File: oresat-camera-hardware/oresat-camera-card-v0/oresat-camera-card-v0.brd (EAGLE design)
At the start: 99.8 x 94.7 mm, 318 parts, among them J1 J-SAMTEC-TFM-120-X1-XXX-D-RA, J2 DM3BT-DSF-PEJS, J4 3-1734592-64-1734592-0, J8 2-1734592-0, Q1 DMP2240UDM, Q3 MIC842, Q4 MIC842, Q5 PMV45EN, Q6 MOSFET-PCH-SOT23-6, Q7 MOSFET-PCH-SOT23-6, Q8 PMV45EN, Q9 MMBT2907, U1 MAX7310ATE, U10 SN74LVC8T245MPWREPPW24-M, U11 RCLAMP0504FB, U12 RCLAMP0504FB, U13 TPS2051CDBVR, U14 TLVH431, U15 SN74LVC1G07DCK, U2 TPS62112, U3 MAX4211CETE, U4 TCAN330, U5 CLVCH16T245MDGGREP, U6 OSD3358-512M-BSM, U7 TCA9509DGKRDGK8-M, U9 TLV70028QDDCRQ1, Y1 24MHz

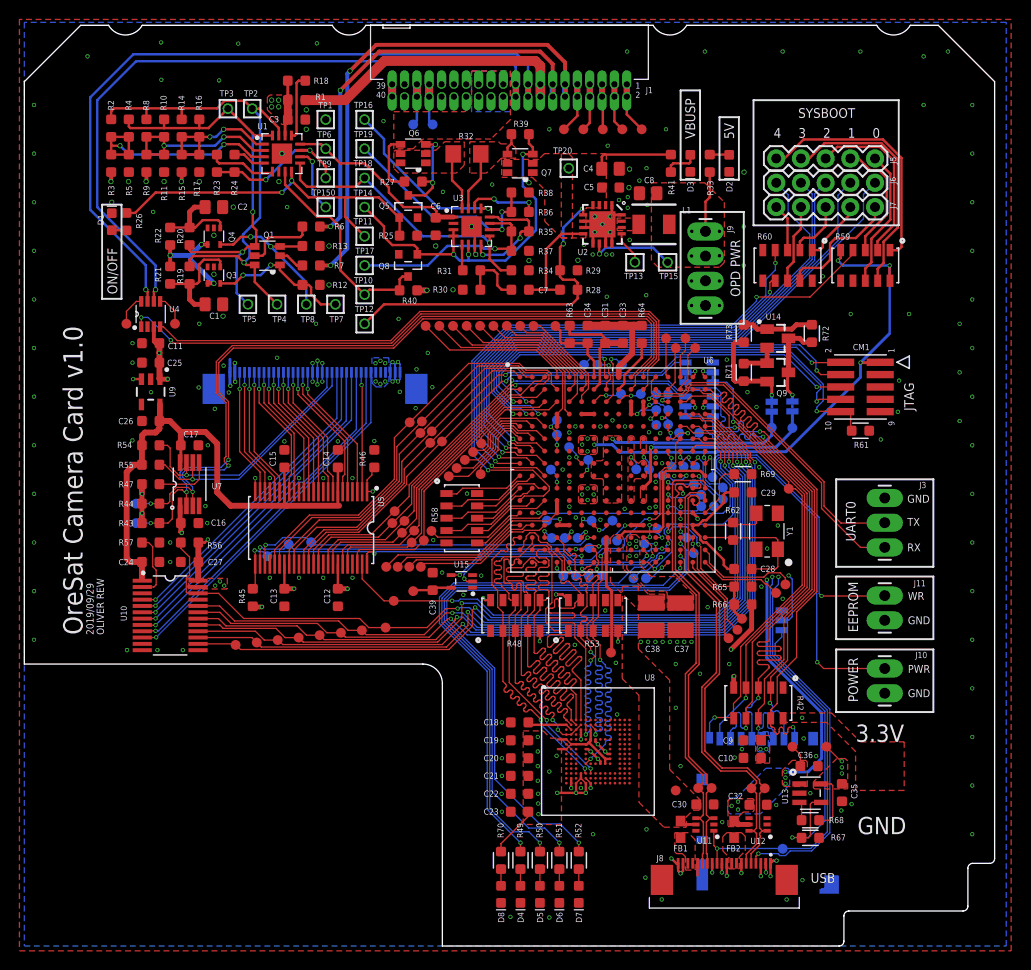
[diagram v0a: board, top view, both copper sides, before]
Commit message: moar VIAS
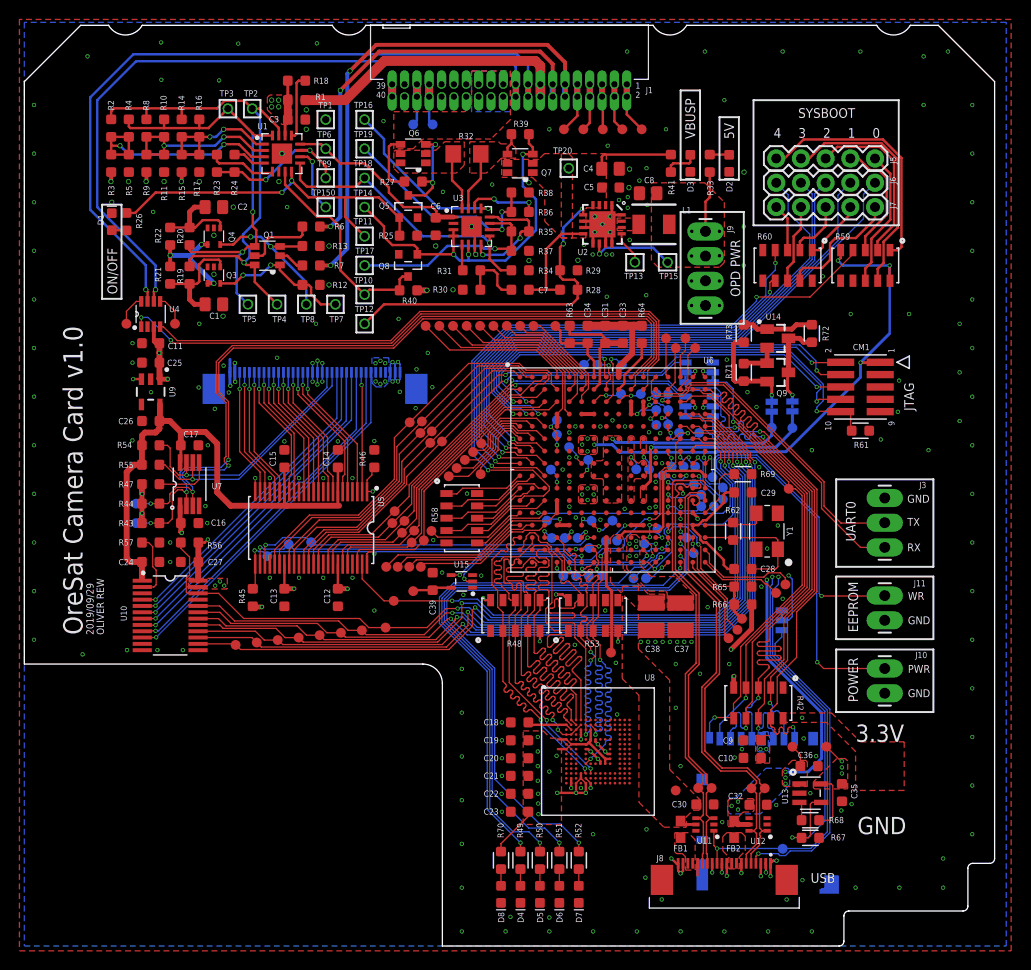
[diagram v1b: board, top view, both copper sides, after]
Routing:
- net GND: vias 244 -> 268
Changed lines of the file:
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@@
 <setting verticaltext="up"/>
 </settings>
-<grid distance="0.5" unitdist="mm" unit="mm" style="lines" multiple="1" display="yes" altdistance="0.0625" altunitdist="mm" altunit="mm"/>
+<grid distance="1.5" unitdist="mm" unit="mm" style="lines" multiple="1" display="yes" altdistance="0.0625" altunitdist="mm" altunit="mm"/>
 <layers>
 <layer number="1" name="Top" color="4" fill="1" visible="yes" active="yes"/>
@@
 <via x="36.9375" y="84.84375" extent="1-16" drill="0.254"/>
 <via x="26.1875" y="78.625" extent="1-16" drill="0.35"/>
+<via x="45" y="1.5" extent="1-16" drill="0.254"/>
+<via x="49.5" y="1.5" extent="1-16" drill="0.254"/>
+<via x="54" y="1.5" extent="1-16" drill="0.254"/>
+<via x="58.5" y="1.5" extent="1-16" drill="0.254"/>
+<via x="63" y="1.5" extent="1-16" drill="0.254"/>
+<via x="67.5" y="1.5" extent="1-16" drill="0.254"/>
+<via x="72" y="1.5" extent="1-16" drill="0.254"/>
+<via x="76.5" y="1.5" extent="1-16" drill="0.254"/>
+<via x="81" y="1.5" extent="1-16" drill="0.254"/>
+<via x="85.5" y="6" extent="1-16" drill="0.254"/>
+<via x="90" y="6" extent="1-16" drill="0.254"/>
+<via x="94.5" y="6" extent="1-16" drill="0.254"/>
+<via x="94.5" y="9" extent="1-16" drill="0.254"/>
+<via x="45" y="6" extent="1-16" drill="0.254"/>
+<via x="45" y="10.5" extent="1-16" drill="0.254"/>
+<via x="45" y="15" extent="1-16" drill="0.254"/>
+<via x="45" y="19.5" extent="1-16" drill="0.254"/>
+<via x="45" y="24" extent="1-16" drill="0.254"/>
+<via x="45" y="28.5" extent="1-16" drill="0.254"/>
+<via x="6" y="30" extent="1-16" drill="0.254"/>
+<via x="36" y="34.5" extent="1-16" drill="0.254"/>
+<via x="81" y="51" extent="1-16" drill="0.254"/>
+<via x="93" y="51" extent="1-16" drill="0.254"/>
+<via x="72" y="87" extent="1-16" drill="0.254"/>
 </signal>
 <signal name="N$262">

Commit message: small improvements
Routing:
- net N$585: track 48.5 -> 51.2 mm
- net CAN2_L: track 72.5 -> 71.7 mm
- net CAN2_H: track 75.3 -> 74.4 mm
- net VPD: track 51.4 -> 50.9 mm
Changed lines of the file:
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@@
 </element>
 <element name="D1" library="SparkFun-LED" library_urn="urn:adsk.eagle:library:529" package="LED-0603" package3d_urn="urn:adsk.eagle:package:39354/1" value="AMBER" x="9" y="74.5" smashed="yes" rot="R90">
-<attribute name="NAME" x="8.1775" y="74.6875" size="0.635" layer="25" font="vector" ratio="20" rot="R90" align="bottom-center"/>
+<attribute name="NAME" x="7.6775" y="74.5" size="0.635" layer="25" font="vector" ratio="20" rot="R90" align="bottom-center"/>
 <attribute name="PROD_ID" value="" x="146.5" y="49.5" size="1.778" layer="27" rot="R90" display="off"/>
 <attribute name="VALUE" x="9.635" y="74.5" size="0.6096" layer="27" font="vector" ratio="20" rot="R90" align="top-center"/>
@@
 <wire x1="13.5" y1="67.5" x2="13.5" y2="70" width="0.254" layer="16"/>
 <wire x1="13.5" y1="70" x2="7.5" y2="76" width="0.254" layer="16"/>
-<wire x1="7.5" y1="76" x2="7.5" y2="87" width="0.254" layer="16"/>
-<wire x1="11.5" y1="91" x2="7.5" y2="87" width="0.254" layer="16"/>
+<wire x1="7.5" y1="76" x2="7.5" y2="85.5" width="0.254" layer="16"/>
+<wire x1="13" y1="91" x2="7.5" y2="85.5" width="0.254" layer="16"/>
 <wire x1="50.535" y1="88.629" x2="50.535" y2="90.465" width="0.254" layer="16"/>
 <wire x1="50.535" y1="90.465" x2="50" y2="91" width="0.254" layer="16"/>
-<wire x1="50" y1="91" x2="11.5" y2="91" width="0.254" layer="16"/>
+<wire x1="50" y1="91" x2="13" y2="91" width="0.254" layer="16"/>
 <wire x1="50.535" y1="87.359" x2="50.535" y2="88.629" width="0.6096" layer="1"/>
 <wire x1="50.535" y1="87.359" x2="50.535" y2="88.629" width="0.6096" layer="16"/>
@@
 <wire x1="51.805" y1="90.60125" x2="51.805" y2="88.629" width="0.254" layer="16"/>
 <wire x1="12.5" y1="70" x2="6.78125" y2="75.71875" width="0.254" layer="16"/>
-<wire x1="6.78125" y1="75.71875" x2="6.78125" y2="87.28125" width="0.254" layer="16"/>
-<wire x1="6.78125" y1="87.28125" x2="11.21875" y2="91.71875" width="0.254" layer="16"/>
-<wire x1="11.21875" y1="91.71875" x2="50.6875" y2="91.71875" width="0.254" layer="16"/>
+<wire x1="6.78125" y1="75.71875" x2="6.78125" y2="85.78125" width="0.254" layer="16"/>
+<wire x1="6.78125" y1="85.78125" x2="12.71875" y2="91.71875" width="0.254" layer="16"/>
+<wire x1="12.71875" y1="91.71875" x2="50.6875" y2="91.71875" width="0.254" layer="16"/>
 <wire x1="50.6875" y1="91.71875" x2="51.805" y2="90.60125" width="0.254" layer="16"/>
 <wire x1="51.805" y1="87.359" x2="51.805" y2="88.629" width="0.6096" layer="1"/>
@@
 <wire x1="49.94" y1="63.3565" x2="73.0604375" y2="63.3565" width="0.127" layer="16"/>
 <contactref element="R60" pad="7"/>
-<wire x1="76.6875" y1="67.25" x2="76.6875" y2="66.9835625" width="0.127" layer="16"/>
-<wire x1="76.6875" y1="66.9835625" x2="73.0604375" y2="63.3565" width="0.127" layer="16"/>
-<via x="76.6875" y="67.25" extent="1-16" drill="0.254"/>
-<wire x1="76.6875" y1="67.25" x2="76.6875" y2="68.2577" width="0.127" layer="1"/>
-<wire x1="76.855" y1="68.4252" x2="76.6875" y2="68.2577" width="0.127" layer="1"/>
-<wire x1="76.855" y1="68.4252" x2="77.23" y2="68.4252" width="0.127" layer="1"/>
+<wire x1="77.875" y1="69.5" x2="77.875" y2="68.1710625" width="0.127" layer="16"/>
+<wire x1="77.875" y1="68.1710625" x2="73.0604375" y2="63.3565" width="0.127" layer="16"/>
+<via x="77.875" y="69.5" extent="1-16" drill="0.254"/>
+<wire x1="77.875" y1="69.5" x2="77.4375" y2="69.5" width="0.127" layer="1"/>
+<wire x1="77.23" y1="69.2925" x2="77.23" y2="68.4252" width="0.127" layer="1"/>
+<wire x1="77.4375" y1="69.5" x2="77.23" y2="69.2925" width="0.127" layer="1"/>
 </signal>
 <signal name="N$586">
@@
 <contactref element="R60" pad="4"/>
 <via x="77.25" y="70.25" extent="1-16" drill="0.254"/>
-<wire x1="76.2684" y1="68.5486" x2="77.25" y2="69.5302" width="0.127" layer="16"/>
-<wire x1="76.2684" y1="66.923675" x2="76.2684" y2="68.5486" width="0.127" layer="16"/>
-<wire x1="72.955225" y1="63.6105" x2="76.2684" y2="66.923675" width="0.127" layer="16"/>
-<wire x1="77.25" y1="69.5302" x2="77.25" y2="70.25" width="0.127" layer="16"/>
+<wire x1="77.25" y1="67.905275" x2="77.25" y2="70.25" width="0.127" layer="16"/>
+<wire x1="72.955225" y1="63.6105" x2="77.25" y2="67.905275" width="0.127" layer="16"/>
 <wire x1="77.25" y1="70.25" x2="77.23" y2="70.27" width="0.127" layer="1"/>
 <wire x1="77.23" y1="70.27" x2="77.23" y2="71.5748" width="0.127" layer="1"/>
@@
 <wire x1="49.729575" y1="63.8645" x2="72.8500125" y2="63.8645" width="0.127" layer="16"/>
 <contactref element="R59" pad="4"/>
-<wire x1="75.3125125" y1="66.327" x2="75.3125" y2="66.75" width="0.127" layer="16"/>
-<via x="75.3125" y="66.75" extent="1-16" drill="0.254"/>
-<wire x1="72.8500125" y1="63.8645" x2="75.3125125" y2="66.327" width="0.127" layer="16"/>
-<wire x1="75.3125" y1="66.75" x2="80.8125" y2="66.75" width="0.127" layer="1"/>
+<wire x1="75.8125125" y1="66.827" x2="75.8125" y2="67.25" width="0.127" layer="16"/>
+<via x="75.8125" y="67.25" extent="1-16" drill="0.254"/>
+<wire x1="72.8500125" y1="63.8645" x2="75.8125125" y2="66.827" width="0.127" layer="16"/>
+<wire x1="75.8125" y1="67.25" x2="81.3125" y2="67.25" width="0.127" layer="1"/>
 <wire x1="85.23" y1="71.1675" x2="85.23" y2="71.5748" width="0.127" layer="1"/>
-<wire x1="80.8125" y1="66.75" x2="85.23" y2="71.1675" width="0.127" layer="1"/>
+<wire x1="81.3125" y1="67.25" x2="85.23" y2="71.1675" width="0.127" layer="1"/>
 </signal>
 <signal name="N$602">
@@
 <wire x1="82.875" y1="72.25" x2="82.875" y2="70.5625" width="0.254" layer="1"/>
 <wire x1="82.875" y1="70.5625" x2="82.0625" y2="69.75" width="0.254" layer="1"/>
-<wire x1="79.77" y1="69.395" x2="79.77" y2="68.4252" width="0.254" layer="1"/>
+<wire x1="79.77" y1="69.2075" x2="79.77" y2="68.4252" width="0.254" layer="1"/>
 <wire x1="87.5" y1="74.78881875" x2="85.52368125" y2="72.8125" width="0.254" layer="1"/>
 <wire x1="85.52368125" y1="72.8125" x2="83.4375" y2="72.8125" width="0.254" layer="1"/>
 <wire x1="83.4375" y1="72.8125" x2="82.875" y2="72.25" width="0.254" layer="1"/>
-<wire x1="82.0625" y1="69.75" x2="80.125" y2="69.75" width="0.254" layer="1"/>
-<wire x1="80.125" y1="69.75" x2="79.77" y2="69.395" width="0.254" layer="1"/>
+<wire x1="82.0625" y1="69.75" x2="80.3125" y2="69.75" width="0.254" layer="1"/>
+<wire x1="80.3125" y1="69.75" x2="79.77" y2="69.2075" width="0.254" layer="1"/>
 </signal>
 <signal name="N$631">
@@
 <wire x1="25.96875" y1="85" x2="25.4375" y2="85.53125" width="1.016" layer="15"/>
 <wire x1="31" y1="85" x2="32.5" y2="83.5" width="0.6096" layer="15"/>
-<wire x1="36.28125" y1="83.5" x2="40.0625" y2="79.71875" width="0.6096" layer="15"/>
-<wire x1="40.0625" y1="79.71875" x2="40.0625" y2="68.78125" width="0.6096" layer="15"/>
+<wire x1="35.40625" y1="83.5" x2="40.0625" y2="78.84375" width="0.6096" layer="15"/>
+<wire x1="40.0625" y1="78.84375" x2="40.0625" y2="68.78125" width="0.6096" layer="15"/>
 <wire x1="40.0625" y1="68.78125" x2="41.40625" y2="67.4375" width="0.6096" layer="15"/>
 <via x="41.40625" y="67.4375" extent="1-16" drill="0.35"/>
-<wire x1="32.5" y1="83.5" x2="36.28125" y2="83.5" width="0.6096" layer="15"/>
+<wire x1="32.5" y1="83.5" x2="35.40625" y2="83.5" width="0.6096" layer="15"/>
 <wire x1="40.4" y1="67.4375" x2="41.40625" y2="67.4375" width="0.6096" layer="1"/>
 <wire x1="8.9375" y1="79.6" x2="8.9375" y2="78.65625" width="0.4064" layer="1"/>
@@
 <wire x1="16.1875" y1="79.6" x2="16.1875" y2="78.65625" width="0.4064" layer="1"/>
 <wire x1="16.1875" y1="78.65625" x2="16.15625" y2="78.625" width="0.4064" layer="1"/>
+<wire x1="26.15625" y1="86.3125" x2="26.15625" y2="87" width="0" layer="19" extent="1-1"/>
+<wire x1="25.4375" y1="87" x2="26.15625" y2="87" width="0" layer="19" extent="1-1"/>
+<wire x1="25.4375" y1="86.3125" x2="25.4375" y2="87" width="0" layer="19" extent="1-1"/>
+<wire x1="27.1" y1="87" x2="26.15625" y2="87" width="0" layer="19" extent="1-1"/>
+<wire x1="16.1875" y1="79.6" x2="26.825" y2="83.3596" width="0" layer="19" extent="1-1"/>
+<wire x1="12.5625" y1="79.6" x2="16.1875" y2="79.6" width="0" layer="19" extent="1-1"/>
+<wire x1="8.9375" y1="79.6" x2="12.5625" y2="79.6" width="0" layer="19" extent="1-1"/>
+<wire x1="15" y1="72.1" x2="16.15625" y2="78.625" width="0" layer="19" extent="1-1"/>
 </signal>
 <signal name="PB6/SCL">

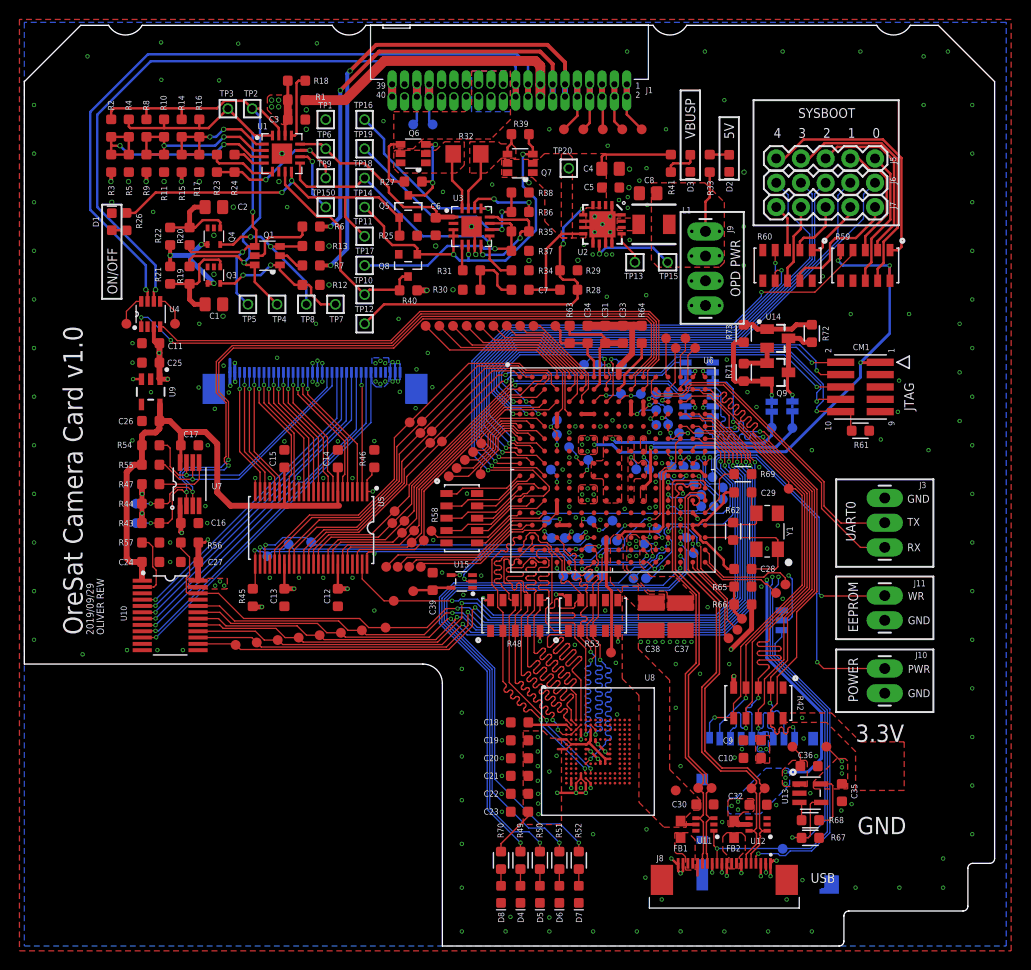
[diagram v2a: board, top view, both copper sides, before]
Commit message: added silk on resistors
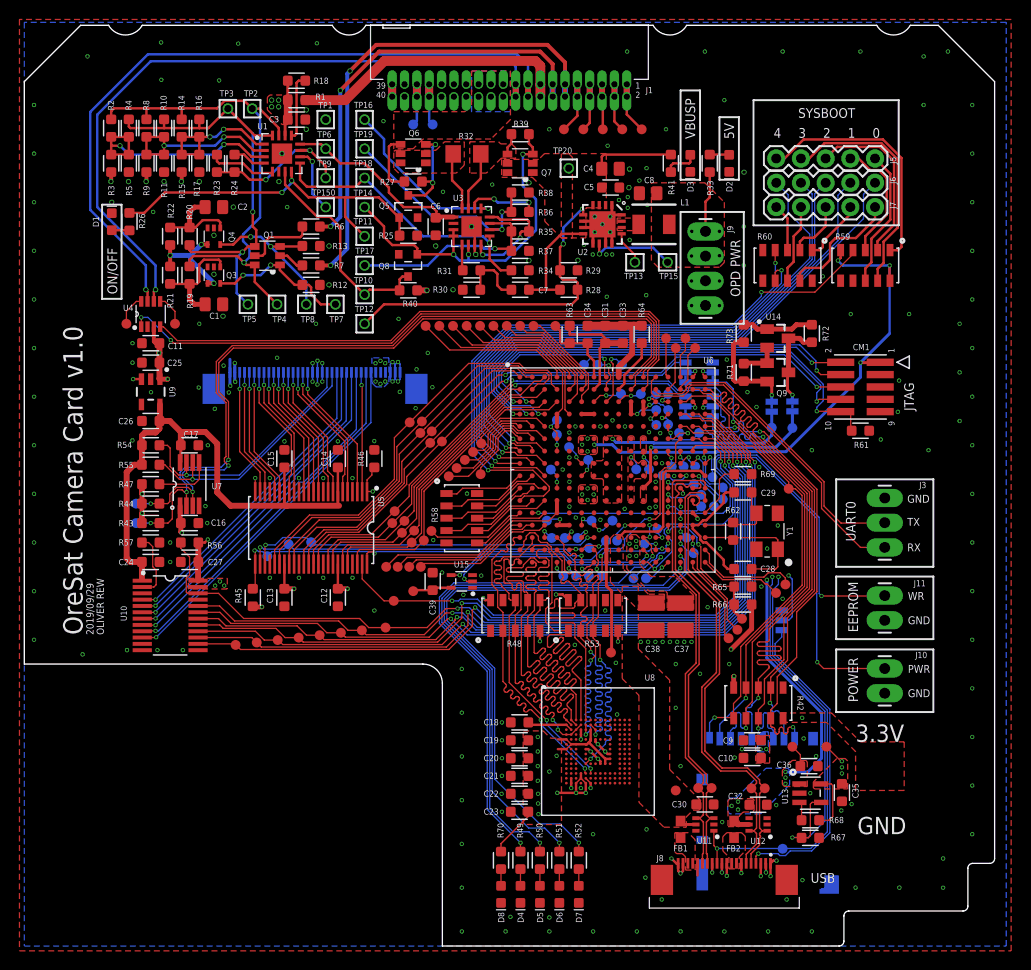
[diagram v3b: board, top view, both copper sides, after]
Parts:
- C10, C11, C12, C13, C14, C15, C16, C17, C18, C19, C20, C21, C22, C23, C24, C25, C26, C27, C28, C29, C3, C30, C32, C35, C36, C39, C5, C6, C7, C9, R1, R10, R11, R12, R13, R14, R15, R16, R17, R18, R19, R2, R20, R21, R22, R23, R24, R25, R26, R27, R28, R29, R3, R30, R31, R33, R34, R35, R36, R37, R38, R39, R4, R40, R41, R43, R44, R45, R46, R47, R5, R54, R55, R56, R57, R6, R63, R64, R65, R66, R7, R8, R9: device oresat-rcl:.0603-A-NOSILK -> oresat-rcl:.0603-A
- moved R26 0.31 mm to (10.8, 74.5)
